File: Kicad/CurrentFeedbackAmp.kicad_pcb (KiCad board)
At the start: 2 copper layers, 200 x 100 mm, 123 parts, among them J1 Test_Etapa_3_Inf, J10 Protecc_Sup_In1, J11 Protecc_Inf_In1, J12 Protecc_Sup_In2, J13 Test_Etapa_3_Inf, J14 Entrada, J15 Salida masa2, J16 Salida tierra, J17 Salida senal, J2 Test_Realim_Out, J3 Salida masa1, J4 Protecc_Sup_Out, J5 Protecc_Inf_Out, J6 Conector Vcc, J7 Conector Vdd, J8 Test_Etapa_3_Inf, J9 Test_Etapa_3_Sup, Q1 TIP42C, Q10 BC858, Q11 BC848, Q12 BC858, Q13 BC559, Q14 BC559, Q15 BC559, Q16 BC549, Q17 BC549, Q18 BC549, Q19 BC559, Q2 BD135, Q20 BC549, Q21 BC559, Q22 BC549, Q23 BC848, Q24 BD136, Q25 BC858, Q26 BC848, Q27 BC848, Q28 BC848, Q29 BC858, Q3 BD136, Q30 BC858, Q31 BC848, Q32 BC858, Q33 BD135, Q34 TIP41C, Q35 BC858, Q36 BC848, Q37 BC848, Q38 BC848, Q4 BC848, Q40 BC858, Q41 BC858, Q5 BC848, Q6 BC858, Q7 BC858, Q8 BC848, Q9 BC858, U1 LM7812_TO220, U2 TL082, U3 LM7912_TO220, U4 LM7805_TO220, U5 LM7905_TO220

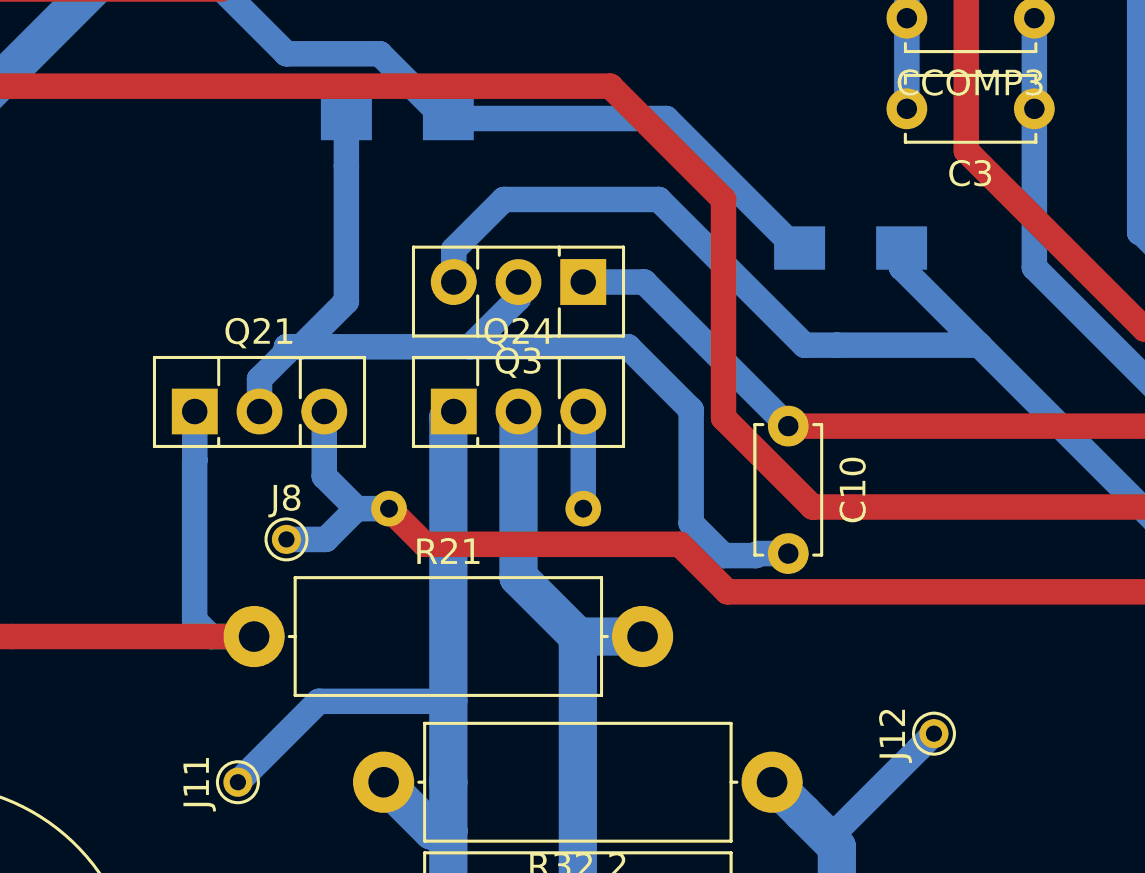
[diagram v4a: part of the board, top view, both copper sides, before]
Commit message: Movimos para arriba los transistores del multiplicador asi podemos llegar a tener una unica chapita
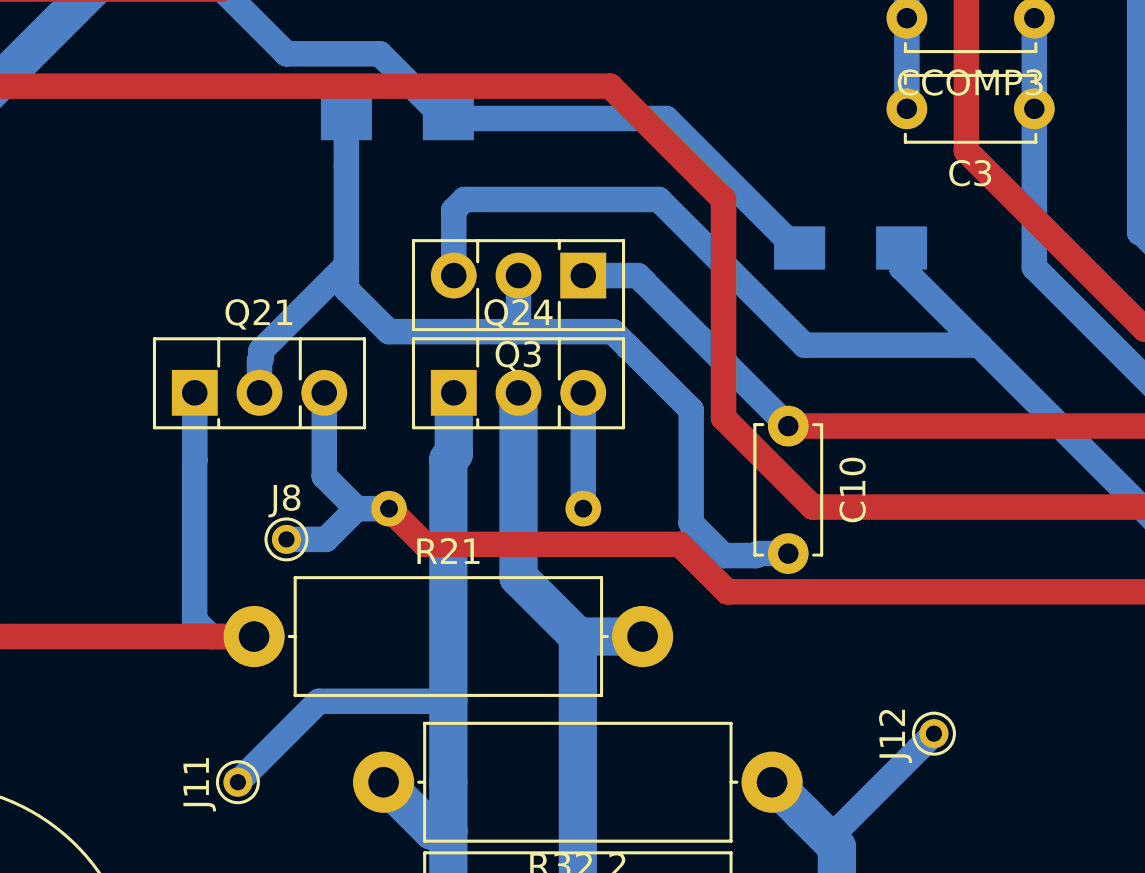
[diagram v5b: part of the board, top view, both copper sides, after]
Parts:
- moved Q21 0.73 mm to (47.2, 76.8)
- moved Q24 0.73 mm to (57.4, 76.8)
- moved Q3 0.25 mm to (62.4, 72.2)
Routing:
- net Net-(C10-Pad2): track 42.3 -> 39.7 mm
- net Vdd: track 201.9 -> 202.6 mm
- net Net-(J8-Pad1): track 144.7 -> 145.4 mm
- net Net-(J11-Pad1): track 51.0 -> 51.7 mm
- net Net-(Q24-Pad3): track 3.81 -> 4.54 mm
- net Net-(J13-Pad1): track 43.4 -> 44.2 mm
- net Net-(Q3-Pad3): track 49.9 -> 50.6 mm

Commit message: Ya va quedando mucho mas prolijo y mas parecido a un amplificador de audio pro
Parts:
- R16, R17: moved to F.Cu
- moved Q15 31.9 mm to (165.0, 82.3)
- moved R3 31.9 mm to (184.8, 77.7)
- moved Q13 31.9 mm to (174.4, 77.5)
- moved R5 31.9 mm to (184.6, 91.7)
- moved Q14 31.9 mm to (174.1, 84.6)
- moved Q19 31.9 mm to (174.4, 91.9)
- moved R4 31.9 mm to (184.6, 84.6)
- moved U4 30.4 mm to (187.1, 49.0)
- moved U3 29.9 mm to (20.3, 61.0)
- moved U5 29.9 mm to (20.3, 48.3)
- moved Q16 29.4 mm to (24.0, 77.7)
- moved Q17 29.4 mm to (24.0, 83.6)
- moved Q18 29.4 mm to (33.1, 81.3)
- moved Q22 29.4 mm to (24.0, 89.4)
- moved R10 29.4 mm to (14.1, 89.4)
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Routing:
- net GND: track 542.2 -> 486.8 mm
- net Vdd: track 202.6 -> 151.1 mm, vias 1 -> 0
- net Vcc: track 236.6 -> 202.3 mm
- net Net-(J8-Pad1): track 145.4 -> 135.0 mm
- net Net-(Q15-Pad1): track 58.5 -> 68.6 mm
- net VccTL: track 117.4 -> 107.8 mm
- net Net-(J9-Pad1): track 151.6 -> 160.9 mm
- net Net-(C3-Pad2): track 83.1 -> 89.6 mm
- net VddTL: track 129.8 -> 124.2 mm
- net Net-(Q18-Pad1): track 51.1 -> 55.3 mm
- net Net-(J11-Pad1): track 51.7 -> 47.7 mm
- net Vcc5: track 58.6 -> 55.8 mm
- net Net-(C4-Pad1): track 117.2 -> 115.6 mm
- net Vdd5: track 58.9 -> 57.8 mm
- net Net-(Q23-Pad1): track 138.5 -> 138.7 mm, vias 6 -> 4

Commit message: ya podemos armar la placa!
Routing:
- net Vcc: track 202.3 -> 187.5 mm
- net GND: track 486.8 -> 500.0 mm
- net Net-(J13-Pad1): track 44.2 -> 48.4 mm
- net Net-(J11-Pad1): track 47.7 -> 50.8 mm
- net Vout: track 199.1 -> 201.3 mm
- net Net-(J10-Pad1): track 46.3 -> 45.7 mm

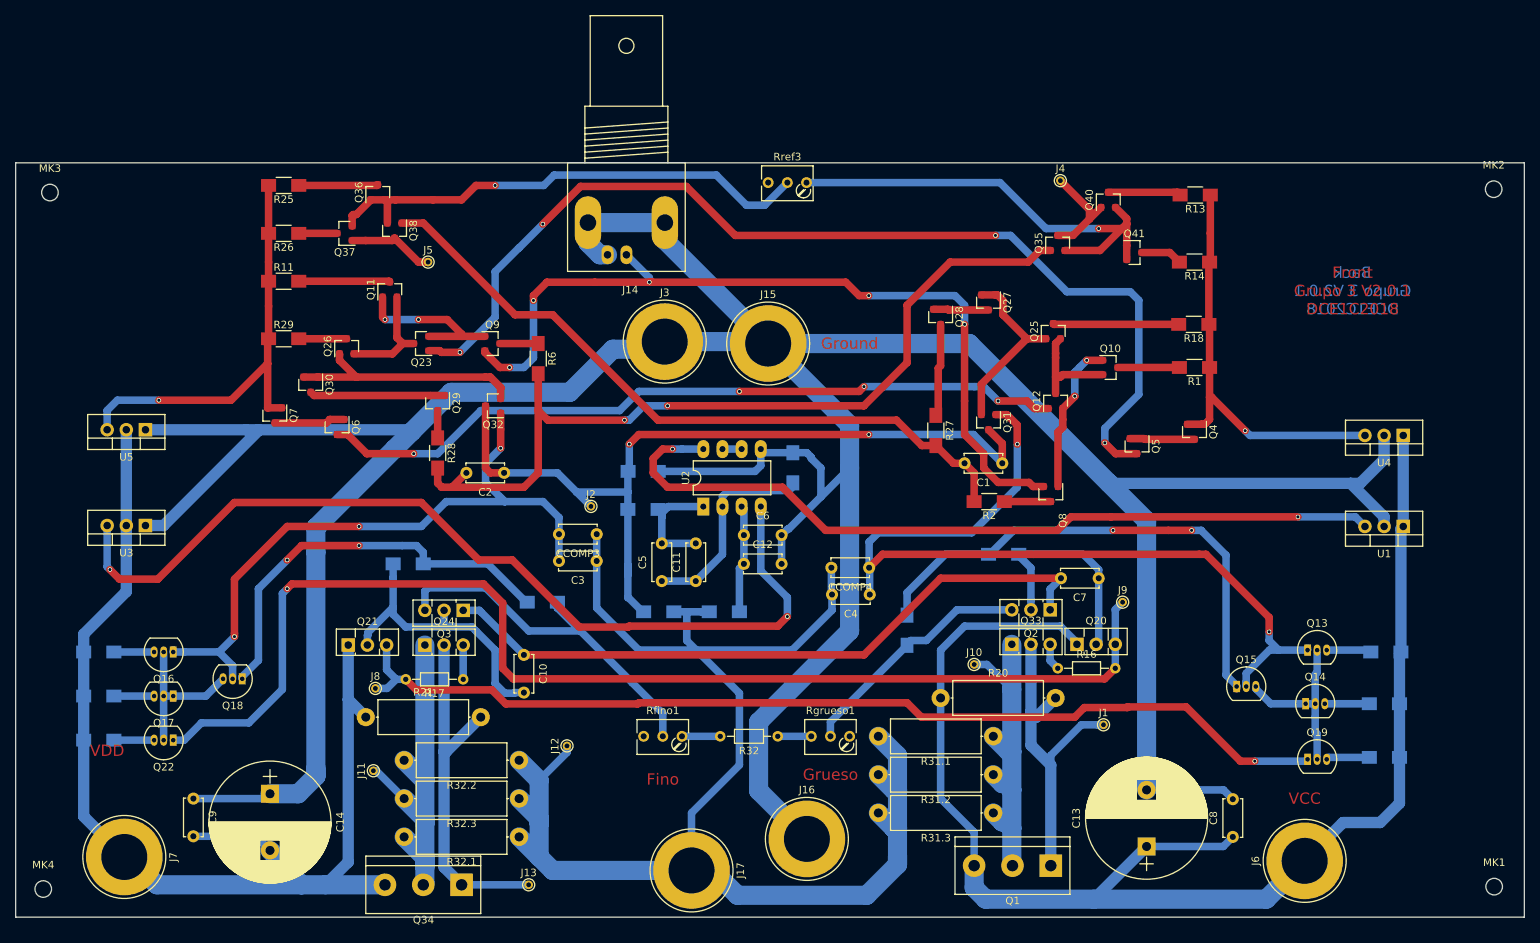
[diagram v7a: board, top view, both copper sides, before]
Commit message: va el circuito sin muchas cosas que sobraban
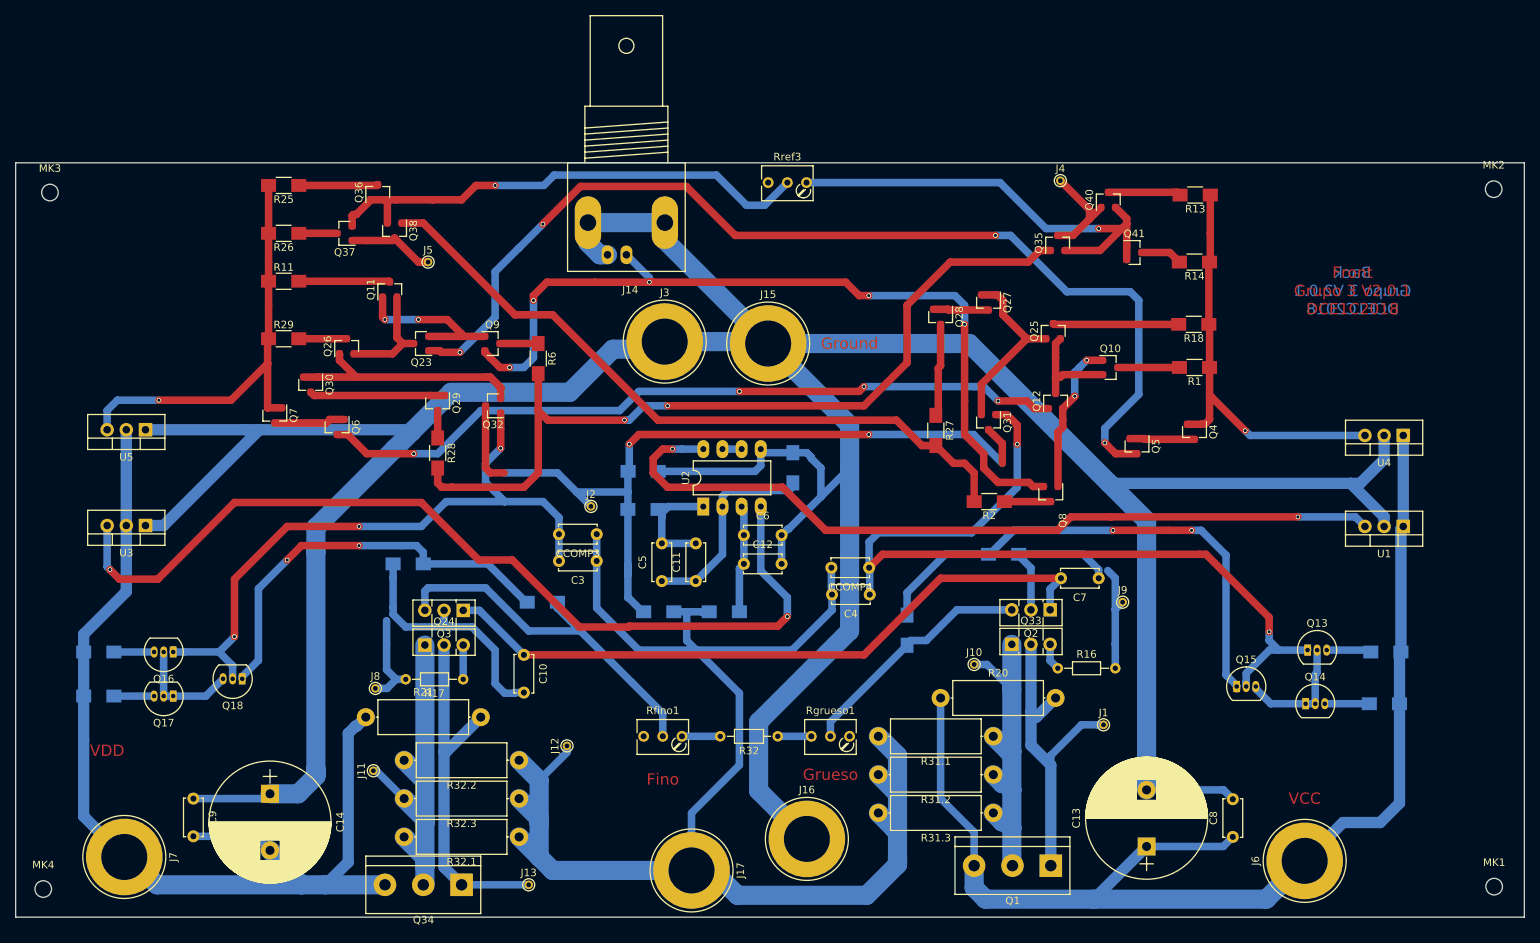
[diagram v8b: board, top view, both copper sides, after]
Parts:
- removed C1, C2: 0.3p, Capacitors_THT:C_Disc_D5.0mm_W2.5mm_P5.00mm
- removed Q19: BC559, TO_SOT_Packages_THT:TO-92_Inline_Narrow_Oval
- removed Q20: BC549, TO_SOT_Packages_THT:TO-126_Vertical
- removed Q21: BC559, TO_SOT_Packages_THT:TO-126_Vertical
- removed Q22: BC549, TO_SOT_Packages_THT:TO-92_Inline_Narrow_Oval
- removed R10, R5: 150, Resistors_SMD:R_1206_HandSoldering
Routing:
- net Net-(J9-Pad1): track 160.9 -> 14.7 mm, vias 1 -> 0
- net Net-(J8-Pad1): track 135.0 -> 12.8 mm, vias 1 -> 0
- net Vcc: track 187.5 -> 160.6 mm
- net Vdd: track 150.8 -> 139.1 mm
- net Net-(C7-Pad1): track 29.5 -> 20.6 mm
- net Net-(Q13-Pad2): track 23.7 -> 16.2 mm
- net Net-(C10-Pad2): track 39.7 -> 33.2 mm
- net Net-(Q16-Pad2): track 20.5 -> 14.7 mm
- net Net-(Q19-Pad3): track 5.76 -> 0.00 mm
- net Net-(Q22-Pad3): track 5.33 -> 0.00 mm
- net Ireference1: track 114.5 -> 111.8 mm
